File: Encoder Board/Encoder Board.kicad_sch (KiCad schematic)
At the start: 20 parts, among them J1 Conn_02x05_Odd_Even, J2 Conn_02x05_Odd_Even, J3 Conn_01x02_Pin, J4 Conn_01x01_Pin, U1 AM26LV32xD, U2 AM26LV31xD_1

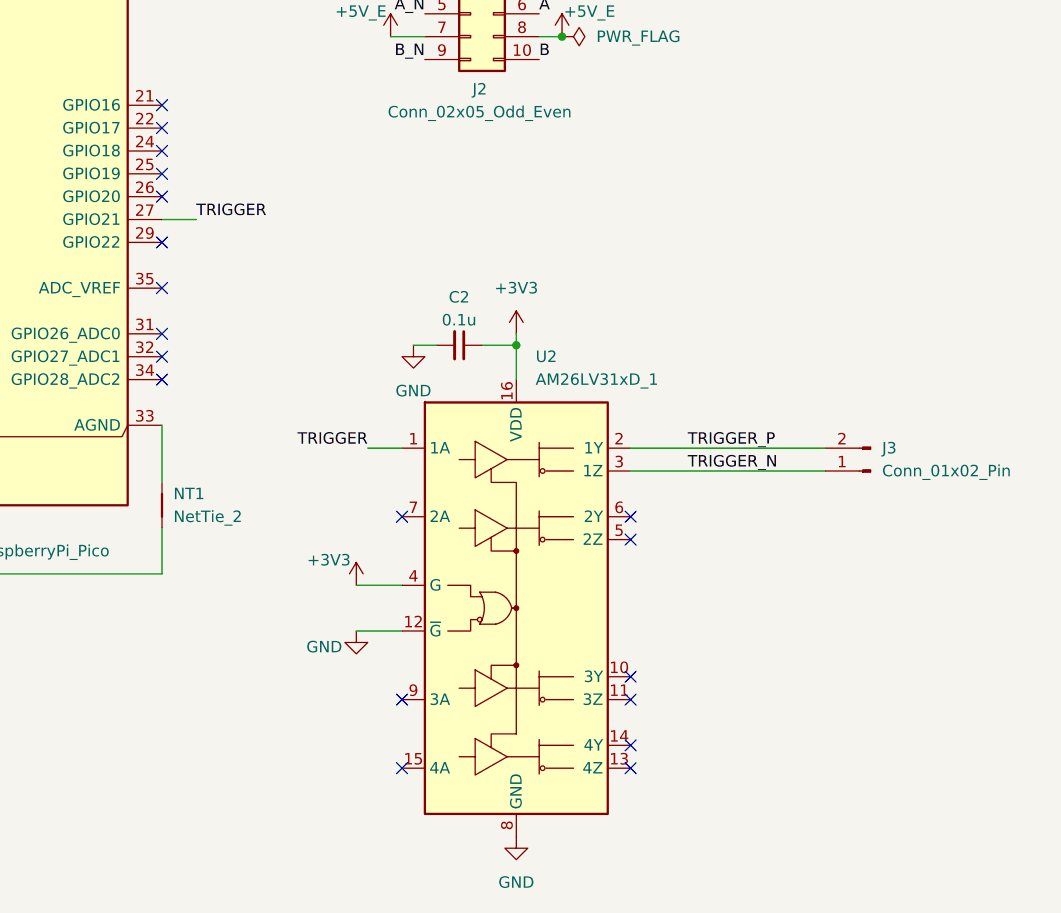
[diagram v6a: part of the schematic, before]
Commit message: remove differential trigger
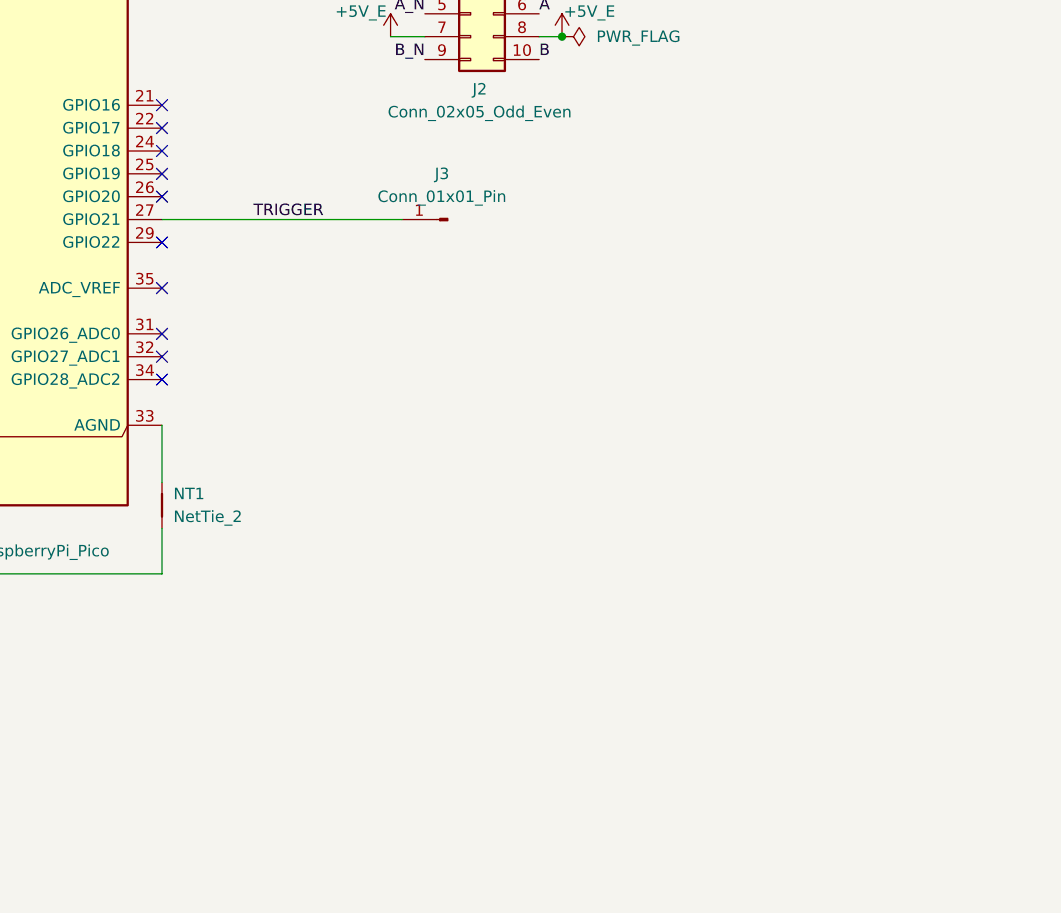
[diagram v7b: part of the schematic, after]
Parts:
- removed C2: 0.1u, Capacitor_SMD:C_0805_2012Metric_Pad1.18x1.45mm_HandSolder, symbol Device:C_Small
- removed J3: Conn_01x02_Pin, Connector_PinHeader_2.00mm:PinHeader_1x02_P2.00mm_Vertical, symbol Connector:Conn_01x02_Pin
- removed U2: AM26LV31xD_1, Package_SO:SOIC-16_3.9x9.9mm_P1.27mm, symbol Interface:AM26LV31xD_1
- added J3: Conn_01x01_Pin, Connector_PinHeader_2.54mm:PinHeader_1x01_P2.54mm_Vertical, symbol Connector:Conn_01x01_Pin
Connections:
- net TRIGGER: now also J3.1 (Pin_1)
- no-connect marks 38 -> 29

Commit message: Update DRC from PCBWay
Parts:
- +3V3_1, +5V_S1, GND_1: footprint TestPoint:TestPoint_Pad_D2.0mm -> TestPoints_WideSM:TestPoint_Pad_D2.0mm_WideSM
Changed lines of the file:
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@@
 			)
 		)
-		(property "Footprint" "TestPoint:TestPoint_Pad_D2.0mm"
+		(property "Footprint" "TestPoints_WideSM:TestPoint_Pad_D2.0mm_WideSM"
 			(at 165.1 99.06 0)
 			(hide yes)
@@
 			)
 		)
-		(property "Footprint" "TestPoint:TestPoint_Pad_D2.0mm"
+		(property "Footprint" "TestPoints_WideSM:TestPoint_Pad_D2.0mm_WideSM"
 			(at 170.18 31.75 0)
 			(hide yes)
@@
 			)
 		)
-		(property "Footprint" "TestPoint:TestPoint_Pad_D2.0mm"
+		(property "Footprint" "TestPoints_WideSM:TestPoint_Pad_D2.0mm_WideSM"
 			(at 144.78 24.13 0)
 			(hide yes)
